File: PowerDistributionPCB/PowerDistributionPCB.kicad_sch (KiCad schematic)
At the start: 38 parts, among them J1 USB3_A, Q1 AOD4185, U1 AP63203WU

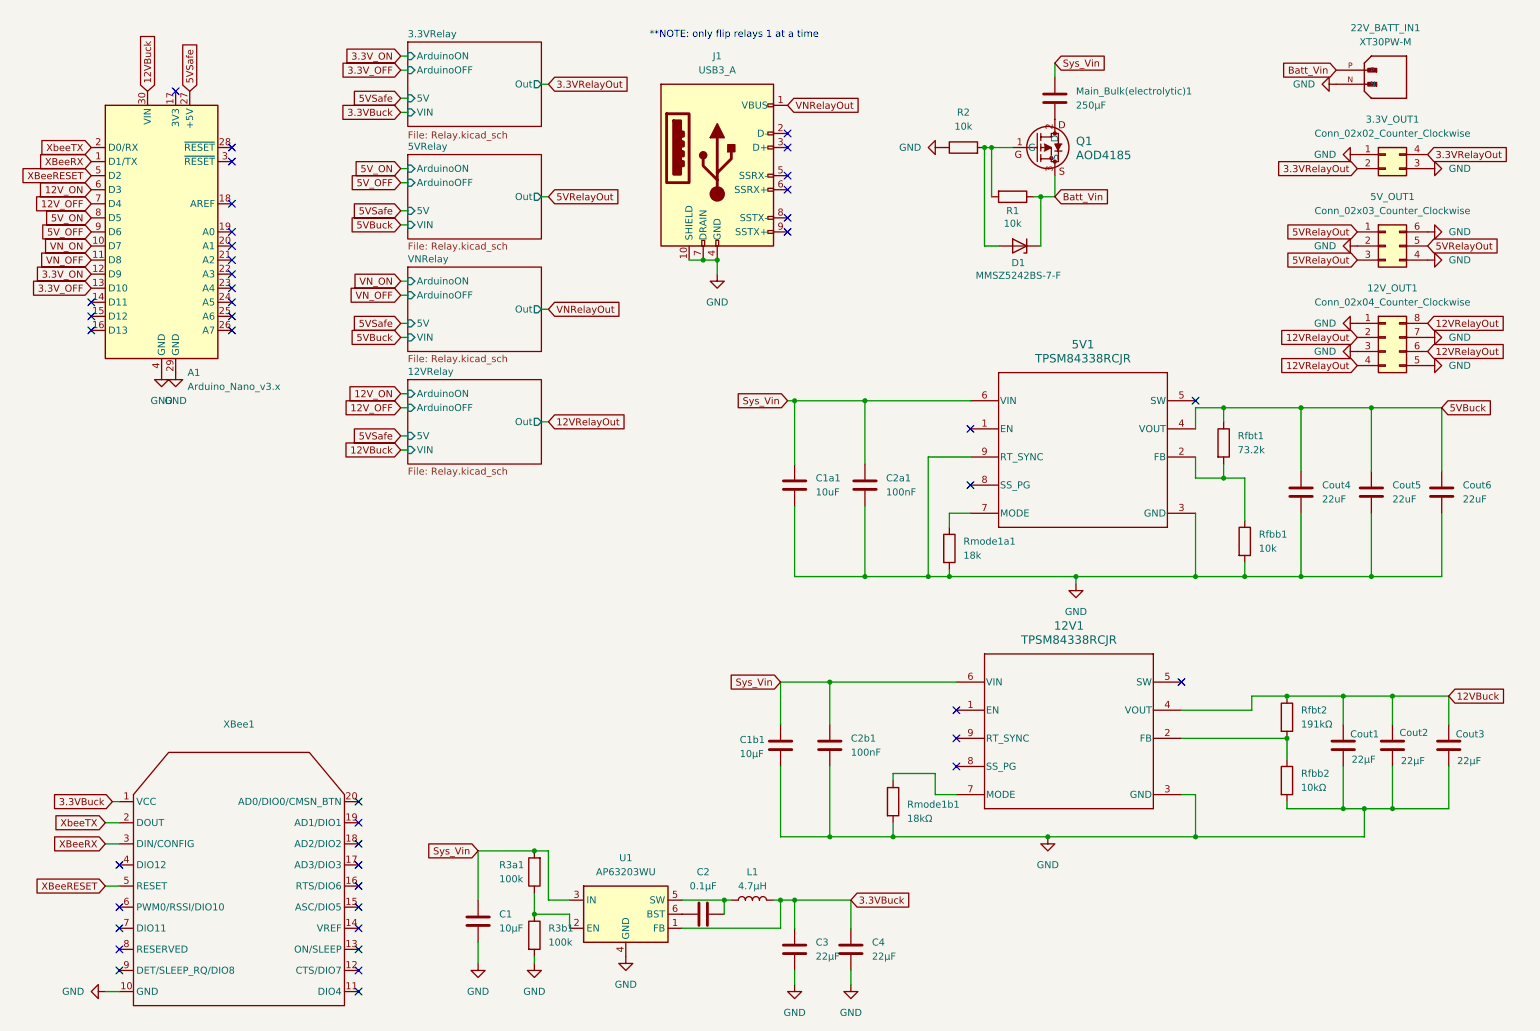
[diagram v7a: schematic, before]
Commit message: added voltage divider and resolved erc issues
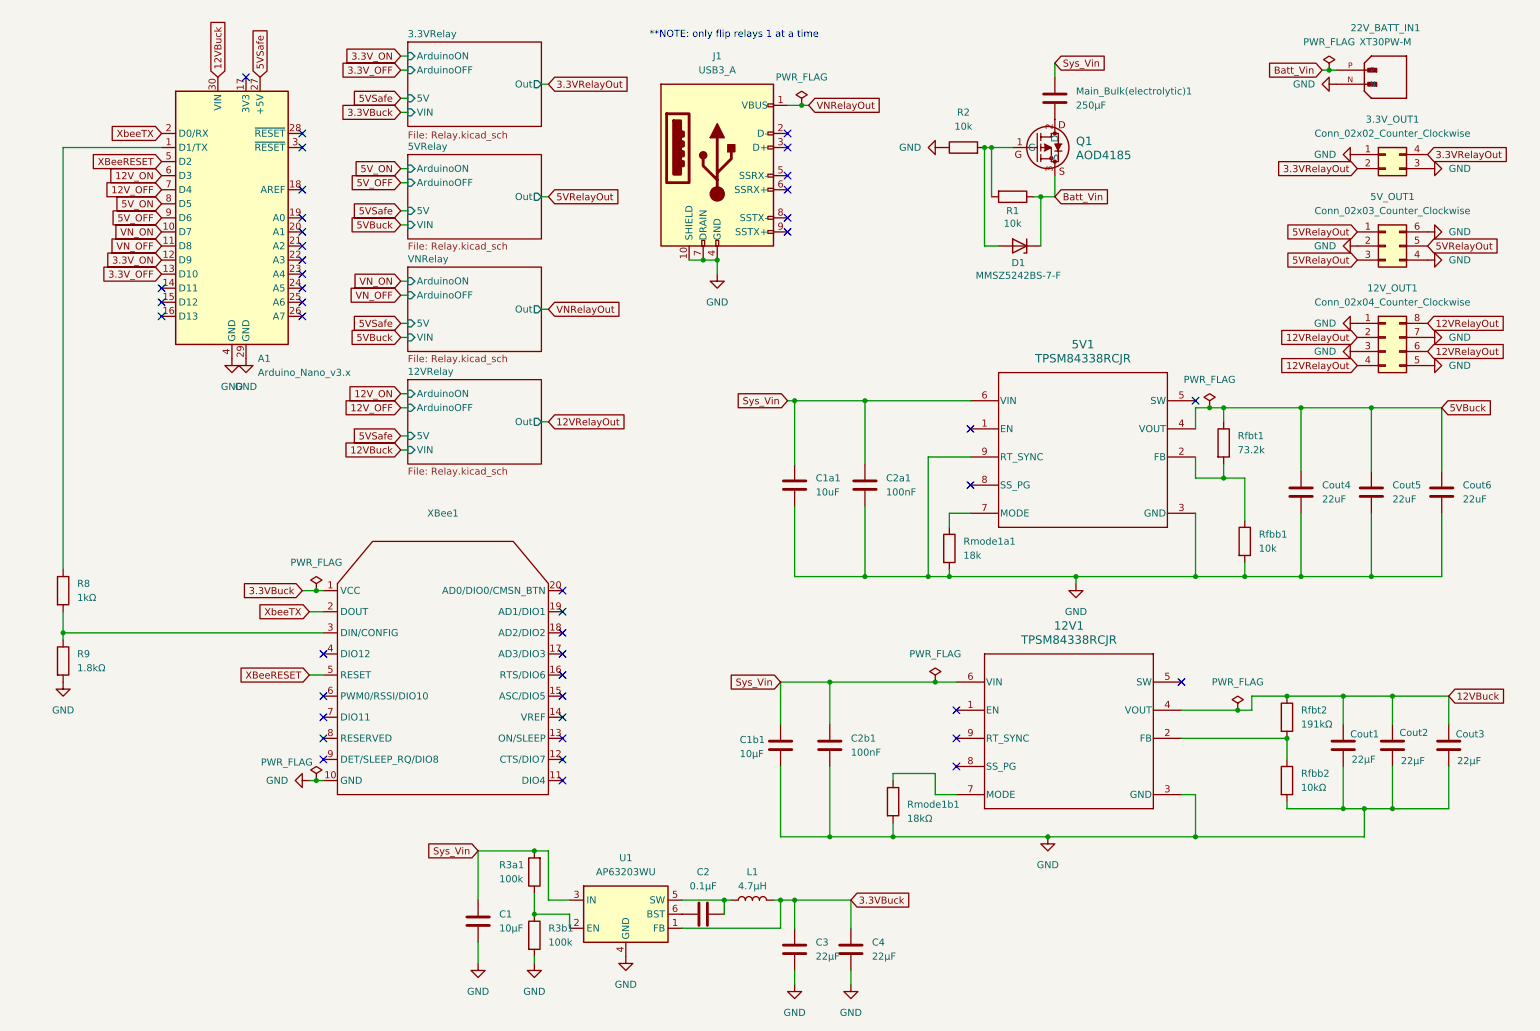
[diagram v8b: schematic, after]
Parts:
- added R8: 1kΩ, Resistor_SMD:R_0805_2012Metric_Pad1.20x1.40mm_HandSolder, symbol Device:R
- added R9: 1.8kΩ, Resistor_SMD:R_0805_2012Metric_Pad1.20x1.40mm_HandSolder, symbol Device:R
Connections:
- net GND: now also R9.2
- net XBeeRX: no longer names the net of XBee1.3 (DIN/CONFIG)
- net XBeeRX: now also R8.2, R9.1; no longer A1.1 (D1/TX)
- new net: A1.1 (D1/TX), R8.1
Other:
- moved on the sheet: A1, XBee1
